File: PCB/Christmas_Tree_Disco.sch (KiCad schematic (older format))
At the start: 0 parts

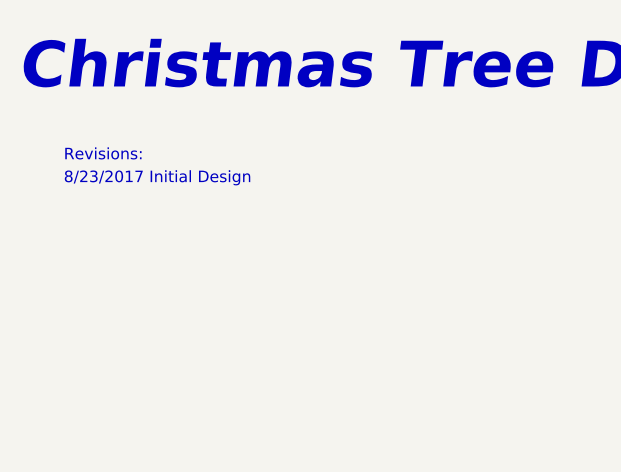
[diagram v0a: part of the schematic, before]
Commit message: Footprint Modifications
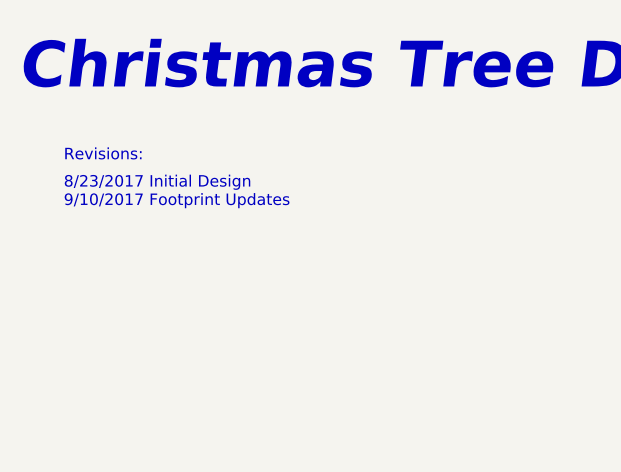
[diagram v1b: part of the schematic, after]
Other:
- note added: "8/23/2017 Initial Design\n9/10/2017 Footprint Updates"
- note removed: "8/23/2017 Initial Design"
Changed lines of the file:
@@
 Sheet 1 20
 Title "Christmas Tree Disco"
-Date "2017-08-23"
-Rev "V1.0"
+Date "2017-09-10"
+Rev "V1.1"
 Comp "www.GitHub.com/Cryochasm"
 Comment1 ""
@@
 Text Notes 1000 1400 0    50   ~ 0
 Revisions:
-Text Notes 1000 1500 0    50   ~ 0
-8/23/2017 Initial Design
+Text Notes 1000 1600 0    50   ~ 0
+8/23/2017 Initial Design\n9/10/2017 Footprint Updates
 $Bitmap
 Pos 9900 6100

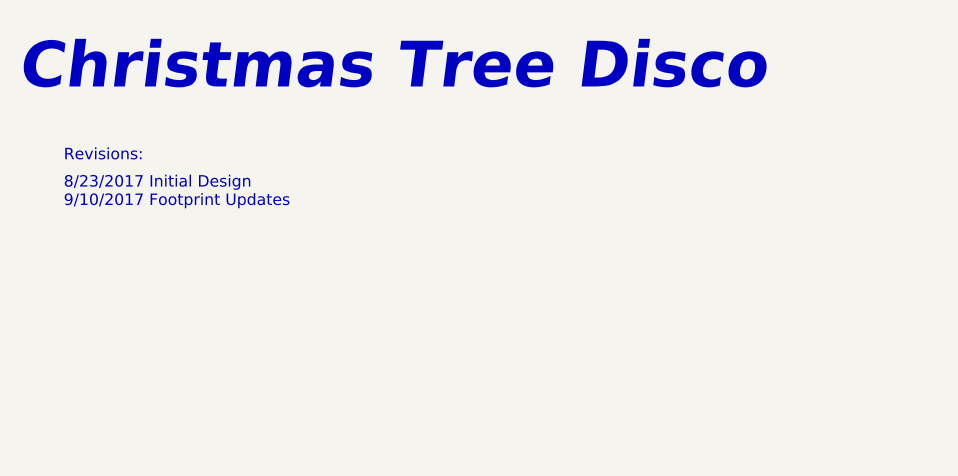
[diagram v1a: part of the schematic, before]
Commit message: Schematic V2
REQUIRES CHANGE TO SOFTWARE: Changed pin of LAT from D7 to D0 to avoid
using the non-maskable interrupt pin.

Added a SMD LED D8 to provide and enviornmental lighting effect.

Removed power supply circuit; USB power from the dev board is sufficent
for
LED brightness. Must be plugged into USB 3.0 or a 2A rated supply.

Updated symbol library to use KiBOM and to Lib Version 4.

TODO: Update  PCB
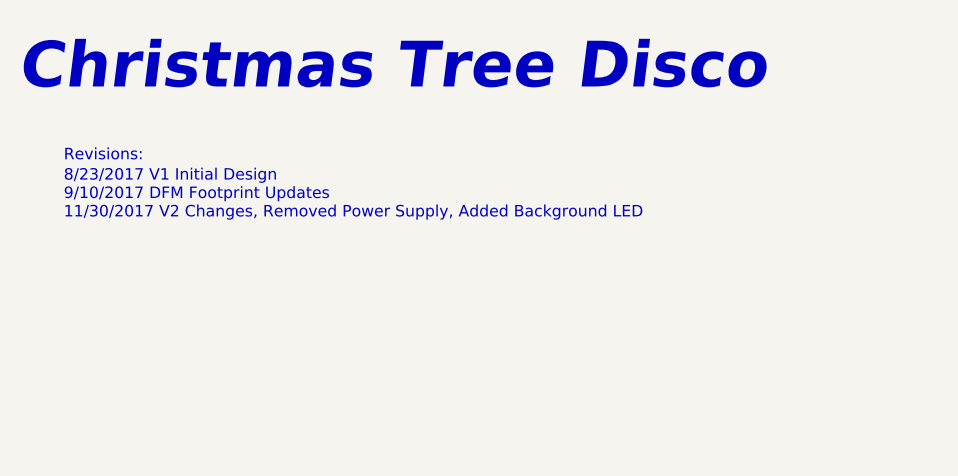
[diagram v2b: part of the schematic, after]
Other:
- note added: "8/23/2017 V1 Initial Design\n9/10/2017 DFM Footprint Updates\n11/30/2017 V2 Changes, Removed Power Supply, Added Background LED"
- note removed: "8/23/2017 Initial Design\n9/10/2017 Footprint Updates"
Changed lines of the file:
@@
-EESchema Schematic File Version 2
+EESchema Schematic File Version 4
 LIBS:local
 LIBS:Christmas_Tree_Disco-cache
@@
 $Descr A 11000 8500
 encoding utf-8
-Sheet 1 20
+Sheet 1 19
 Title "Christmas Tree Disco"
-Date "2017-09-10"
-Rev "V1.1"
+Date "2017-09-20"
+Rev "V2"
 Comp "www.GitHub.com/Cryochasm"
 Comment1 ""
@@
 Text Notes 1000 1400 0    50   ~ 0
 Revisions:
-Text Notes 1000 1600 0    50   ~ 0
-8/23/2017 Initial Design\n9/10/2017 Footprint Updates
+Text Notes 1000 1650 0    50   ~ 0
+8/23/2017 V1 Initial Design\n9/10/2017 DFM Footprint Updates\n11/30/2017 V2 Changes, Removed Power Supply, Added Background LED
 $Bitmap
 Pos 9900 6100
